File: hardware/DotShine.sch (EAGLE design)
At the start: 58 parts, among them CN1 1X4-BIG, IC1 CAT24M010TS, IC3 SI1145, J3 USB-MICROB, U1 ATMEGA328P-MU-QFN32, U2 TMP102, U3 ATSHA204-TSU, X2 MC-RTC-RV-4162-C7-I2C, X3 S4B-ZR

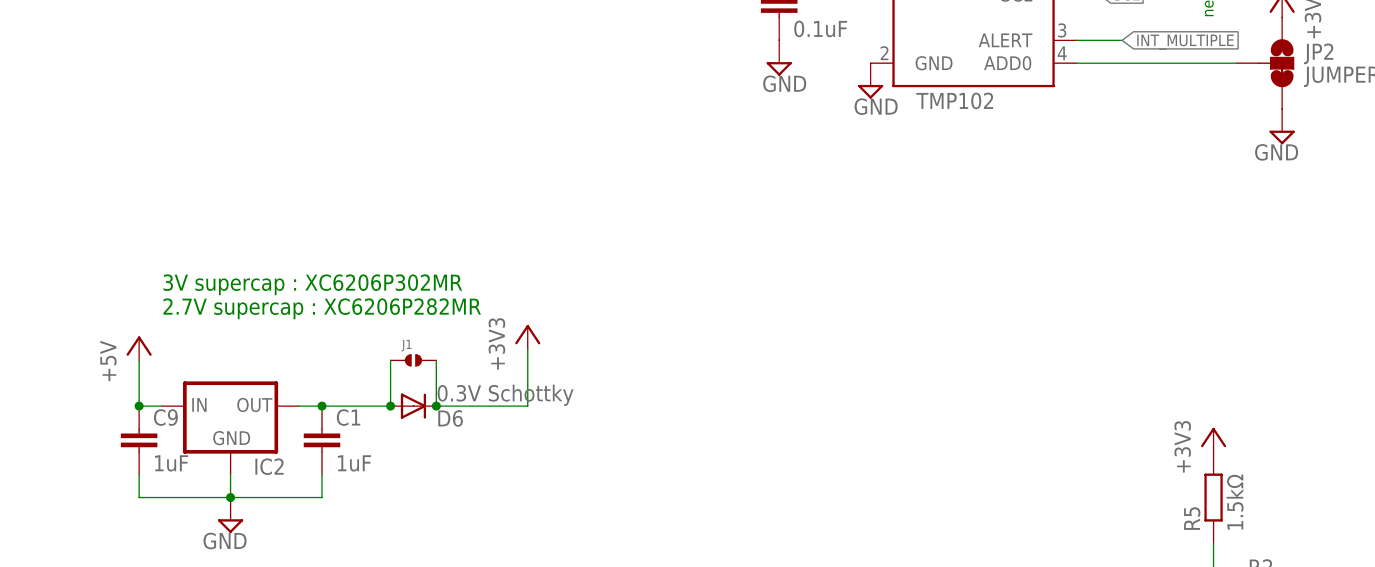
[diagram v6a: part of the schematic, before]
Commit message: Update LDO description
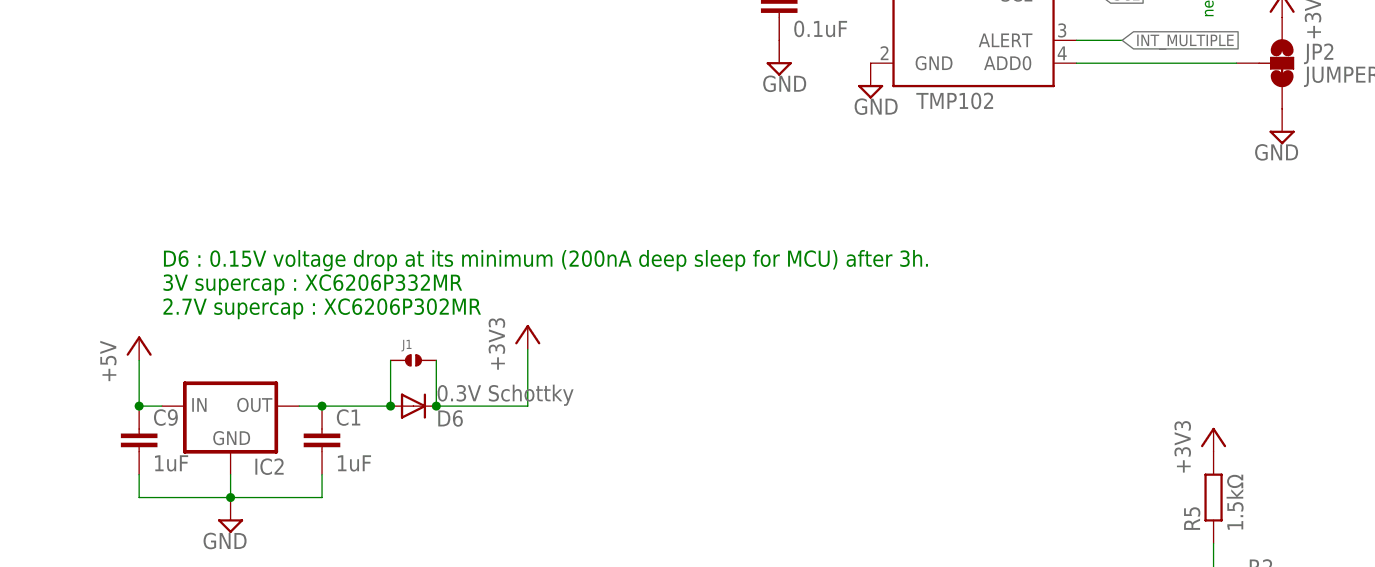
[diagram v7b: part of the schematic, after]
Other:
- note added: "D6 : 0.15V voltage drop at its minimum (200nA deep sleep for MCU) after 3h. 3V supercap : XC6206P332MR 2.7V supercap : XC6206P302MR"
- note removed: "3V supercap : XC6206P302MR 2.7V supercap : XC6206P282MR"
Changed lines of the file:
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@@
 <setting verticaltext="up"/>
 </settings>
-<grid distance="0.05" unitdist="inch" unit="inch" style="lines" multiple="1" display="no" altdistance="0.01" altunitdist="inch" altunit="inch"/>
+<grid distance="0.1" unitdist="inch" unit="inch" style="lines" multiple="1" display="no" altdistance="0.01" altunitdist="inch" altunit="inch"/>
 <layers>
 <layer number="1" name="Top" color="4" fill="1" visible="no" active="no"/>
@@
 <text x="30.48" y="-243.84" size="1.778" layer="91">1000uF .. 6V -&gt; 300uF .. 2V ; 600 .. 3.6V -&gt; buget: 600-300 = 300uF
 1500uF .. 4V -&gt; 750uF .. 2V ; 1350.. 3.6V-&gt; buget: 1350-750 = 600uF</text>
-<text x="137.16" y="-25.4" size="1.778" layer="91">3V supercap : XC6206P302MR
-2.7V supercap : XC6206P282MR</text>
+<text x="137.16" y="-25.4" size="1.778" layer="91">D6 : 0.15V voltage drop at its minimum (200nA deep sleep for MCU) after 3h.
+3V supercap : XC6206P332MR
+2.7V supercap : XC6206P302MR</text>
 <text x="248.92" y="-71.12" size="1.778" layer="91">5V Zener, otherwise
 leakage current too high </text>

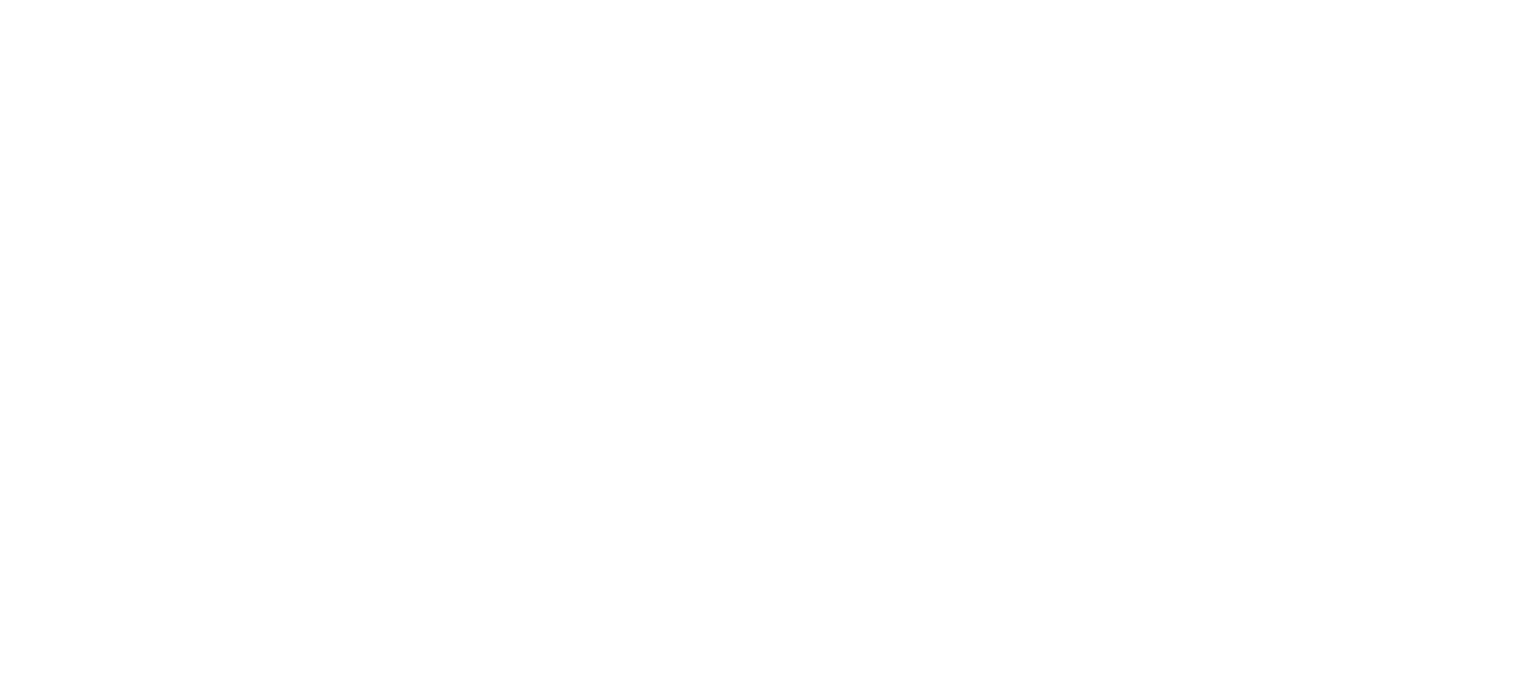
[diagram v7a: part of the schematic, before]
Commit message: Initial version with BLE using JDY-16
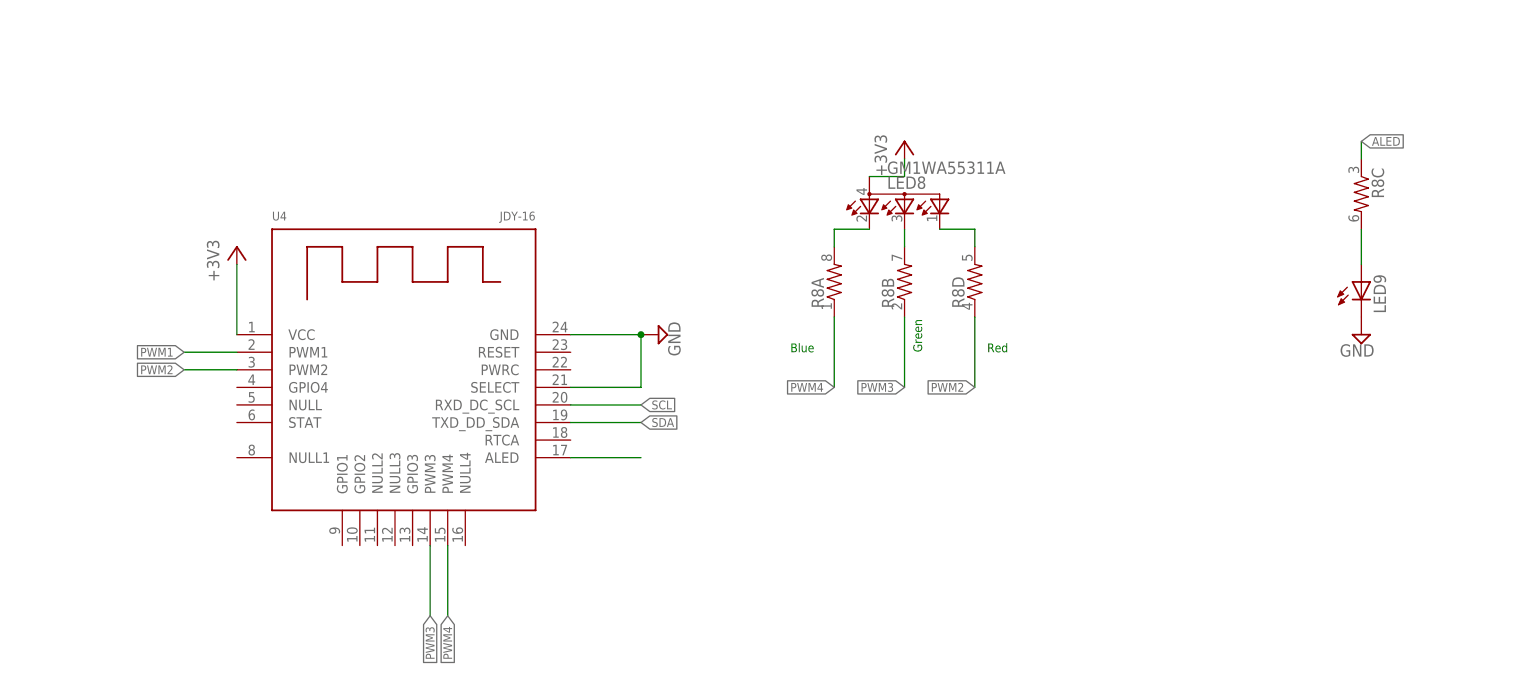
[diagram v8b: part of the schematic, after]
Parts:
- added LED8: GM1WA55311A, led:GM1WA55311A
- added LED9: (no value), SparkFun:LED0603
- added R8: (no value), SparkFun:RESISTOR-ARRAY0603-ARV
- added U4: JDY-16, altro:JDY-16
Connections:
- new net ALED: R8C.1, U4.ALED
- new net BT_BLUE: LED8.CRED, R8A.2
- new net BT_GREEN: LED8.CBLUE, R8B.2
- new net BT_RED: LED8.CGREEN, R8D.2
- new net N$34: LED9.A, R8C.2
- new net PWM1: U4.PWM1
- new net PWM2: R8D.1, U4.PWM2
- new net PWM3: R8B.1, U4.PWM3
- new net PWM4: R8A.1, U4.PWM4
- net +3V3: now also LED8.A, U4.VCC
- net GND: now also LED9.C, U4.GND, U4.SELECT
- net SCL: now also U4.RXD_DC_SCL
- net SDA: now also U4.TXD_DD_SDA
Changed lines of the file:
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@@
 <layer number="154" name="FabDoc2" color="2" fill="1" visible="no" active="no"/>
 <layer number="155" name="FabDoc3" color="7" fill="15" visible="no" active="no"/>
+<layer number="171" name="Fraes_2mm" color="7" fill="1" visible="no" active="yes"/>
 <layer number="199" name="Contour" color="7" fill="1" visible="no" active="no"/>
 <layer number="200" name="200bmp" color="1" fill="10" visible="yes" active="yes"/>
@@
 <part name="+3V17" library="supply1" deviceset="+3V3" device=""/>
 <part name="SUPPLY1" library="supply2" deviceset="GND" device=""/>
+<part name="U4" library="altro" deviceset="JDY-16" device=""/>
+<part name="+3V18" library="supply1" deviceset="+3V3" device=""/>
+<part name="LED8" library="led" deviceset="GM1WA55311A" device=""/>
+<part name="LED9" library="SparkFun" deviceset="LED" device="0603"/>
+<part name="SUPPLY8" library="supply2" deviceset="GND" device=""/>
+<part name="R8" library="SparkFun" deviceset="RESISTOR-ARRAY" device="0603-ARV"/>
+<part name="SUPPLY9" library="supply2" deviceset="GND" device=""/>
+<part name="+3V22" library="supply1" deviceset="+3V3" device=""/>
 </parts>
 <sheets>
@@
 leakage current too high </text>
 <text x="124.46" y="-147.32" size="1.27" layer="91">HW Reset with SW</text>
+<text x="175.26" y="-332.74" size="1.27" layer="91" rot="R90">Green</text>
+<text x="184.658" y="-332.74" size="1.27" layer="91">Red</text>
+<text x="156.21" y="-332.74" size="1.27" layer="91">Blue</text>
 </plain>
 <instances>
@@
 <instance part="+3V17" gate="G$1" x="162.56" y="132.08" rot="R270"/>
 <instance part="SUPPLY1" gate="GND" x="162.56" y="119.38" rot="R90"/>
+<instance part="U4" gate="G$1" x="101.6" y="-337.82"/>
+<instance part="+3V18" gate="G$1" x="172.72" y="-302.26"/>
+<instance part="LED8" gate="G$1" x="172.72" y="-309.88"/>
+<instance part="LED9" gate="G$1" x="238.76" y="-322.58"/>
+<instance part="SUPPLY8" gate="GND" x="238.76" y="-330.2" rot="MR0"/>
+<instance part="R8" gate="A" x="162.56" y="-322.58" rot="R90"/>
+<instance part="R8" gate="B" x="172.72" y="-322.58" rot="R90"/>
+<instance part="R8" gate="C" x="238.76" y="-309.88" rot="R270"/>
+<instance part="R8" gate="D" x="182.88" y="-322.58" rot="R90"/>
+<instance part="SUPPLY9" gate="GND" x="137.16" y="-330.2" rot="MR270"/>
+<instance part="+3V22" gate="G$1" x="76.2" y="-317.5"/>
 </instances>
 <busses>
@@
 <wire x1="160.02" y1="119.38" x2="142.24" y2="119.38" width="0.1524" layer="91"/>
 </segment>
+<segment>
+<pinref part="LED9" gate="G$1" pin="C"/>
+<pinref part="SUPPLY8" gate="GND" pin="GND"/>
+</segment>
+<segment>
+<pinref part="SUPPLY9" gate="GND" pin="GND"/>
+<pinref part="U4" gate="G$1" pin="GND"/>
+<wire x1="134.62" y1="-330.2" x2="124.46" y2="-330.2" width="0.1524" layer="91"/>
+<pinref part="U4" gate="G$1" pin="SELECT"/>
+<wire x1="124.46" y1="-337.82" x2="134.62" y2="-337.82" width="0.1524" layer="91"/>
+<wire x1="134.62" y1="-337.82" x2="134.62" y2="-330.2" width="0.1524" layer="91"/>
+<junction x="134.62" y="-330.2"/>
+</segment>
 </net>
 <net name="SDA" class="0">
@@
 <wire x1="170.18" y1="-210.82" x2="167.64" y2="-210.82" width="0.1524" layer="91"/>
 <label x="167.64" y="-210.82" size="1.27" layer="95" rot="R180" xref="yes"/>
+</segment>
+<segment>
+<pinref part="U4" gate="G$1" pin="TXD_DD_SDA"/>
+<wire x1="124.46" y1="-342.9" x2="134.62" y2="-342.9" width="0.1524" layer="91"/>
+<label x="134.62" y="-342.9" size="1.27" layer="95" xref="yes"/>
 </segment>
 </net>
@@
 <wire x1="160.02" y1="132.08" x2="142.24" y2="132.08" width="0.1524" layer="91"/>
 </segment>
+<segment>
+<pinref part="LED8" gate="G$1" pin="A"/>
+<pinref part="+3V18" gate="G$1" pin="+3V3"/>
+<wire x1="167.64" y1="-307.34" x2="172.72" y2="-307.34" width="0.1524" layer="91"/>
+<wire x1="172.72" y1="-307.34" x2="172.72" y2="-304.8" width="0.1524" layer="91"/>
+</segment>
+<segment>
+<pinref part="+3V22" gate="G$1" pin="+3V3"/>
+<pinref part="U4" gate="G$1" pin="VCC"/>
+<wire x1="76.2" y1="-320.04" x2="76.2" y2="-330.2" width="0.1524" layer="91"/>
+</segment>
 </net>
 <net name="ADCENA" class="0">
@@
 <wire x1="170.18" y1="-215.9" x2="167.64" y2="-215.9" width="0.1524" layer="91"/>
 <label x="167.64" y="-215.9" size="1.27" layer="95" rot="R180" xref="yes"/>
+</segment>
+<segment>
+<pinref part="U4" gate="G$1" pin="RXD_DC_SCL"/>
+<wire x1="124.46" y1="-340.36" x2="134.62" y2="-340.36" width="0.1524" layer="91"/>
+<label x="134.62" y="-340.36" size="1.27" layer="95" xref="yes"/>
 </segment>
 </net>
@@
 </segment>
 </net>
+<net name="BT_RED" class="0">
+<segment>
+<pinref part="R8" gate="D" pin="2"/>
+<pinref part="LED8" gate="G$1" pin="CGREEN"/>
+<wire x1="182.88" y1="-317.5" x2="182.88" y2="-314.96" width="0.1524" layer="91"/>
+<wire x1="182.88" y1="-314.96" x2="177.8" y2="-314.96" width="0.1524" layer="91"/>
+</segment>
+</net>
+<net name="N$34" class="0">
+<segment>
+<pinref part="R8" gate="C" pin="2"/>
+<pinref part="LED9" gate="G$1" pin="A"/>
+<wire x1="238.76" y1="-314.96" x2="238.76" y2="-320.04" width="0.1524" layer="91"/>
+</segment>
+</net>
+<net name="BT_GREEN" class="0">
+<segment>
+<pinref part="LED8" gate="G$1" pin="CBLUE"/>
+<pinref part="R8" gate="B" pin="2"/>
+<wire x1="172.72" y1="-317.5" x2="172.72" y2="-314.96" width="0.1524" layer="91"/>
+</segment>
+</net>
+<net name="BT_BLUE" class="0">
+<segment>
+<pinref part="LED8" gate="G$1" pin="CRED"/>
+<pinref part="R8" gate="A" pin="2"/>
+<wire x1="167.64" y1="-314.96" x2="162.56" y2="-314.96" width="0.1524" layer="91"/>
+<wire x1="162.56" y1="-314.96" x2="162.56" y2="-317.5" width="0.1524" layer="91"/>
+</segment>
+</net>
+<net name="PWM1" class="0">
+<segment>
+<pinref part="U4" gate="G$1" pin="PWM1"/>
+<wire x1="76.2" y1="-332.74" x2="68.58" y2="-332.74" width="0.1524" layer="91"/>
+<label x="68.58" y="-332.74" size="1.27" layer="95" rot="R180" xref="yes"/>
+</segment>
+</net>
+<net name="PWM2" class="0">
+<segment>
+<pinref part="U4" gate="G$1" pin="PWM2"/>
+<wire x1="76.2" y1="-335.28" x2="68.58" y2="-335.28" width="0.1524" layer="91"/>
+<label x="68.58" y="-335.28" size="1.27" layer="95" rot="R180" xref="yes"/>
+</segment>
+<segment>
+<pinref part="R8" gate="D" pin="1"/>
+<wire x1="182.88" y1="-327.66" x2="182.88" y2="-337.82" width="0.1524" layer="91"/>
+<label x="182.88" y="-337.82" size="1.27" layer="95" rot="R180" xref="yes"/>
+</segment>
+</net>
+<net name="PWM3" class="0">
+<segment>
+<pinref part="U4" gate="G$1" pin="PWM3"/>
+<wire x1="104.14" y1="-360.68" x2="104.14" y2="-370.84" width="0.1524" layer="91"/>
+<label x="104.14" y="-370.84" size="1.27" layer="95" rot="R270" xref="yes"/>
+</segment>
+<segment>
+<pinref part="R8" gate="B" pin="1"/>
+<wire x1="172.72" y1="-327.66" x2="172.72" y2="-337.82" width="0.1524" layer="91"/>
+<label x="172.72" y="-337.82" size="1.27" layer="95" rot="R180" xref="yes"/>
+</segment>
+</net>
+<net name="PWM4" class="0">
+<segment>
+<pinref part="U4" gate="G$1" pin="PWM4"/>
+<wire x1="106.68" y1="-360.68" x2="106.68" y2="-370.84" width="0.1524" layer="91"/>
+<label x="106.68" y="-370.84" size="1.27" layer="95" rot="R270" xref="yes"/>
+</segment>
+<segment>
+<pinref part="R8" gate="A" pin="1"/>
+<wire x1="162.56" y1="-327.66" x2="162.56" y2="-337.82" width="0.1524" layer="91"/>
+<label x="162.56" y="-337.82" size="1.27" layer="95" rot="R180" xref="yes"/>
+</segment>
+</net>
+<net name="ALED" class="0">
+<segment>
+<pinref part="R8" gate="C" pin="1"/>
+<wire x1="238.76" y1="-304.8" x2="238.76" y2="-302.26" width="0.1524" layer="91"/>
+<label x="238.76" y="-302.26" size="1.27" layer="95" xref="yes"/>
+</segment>
+<segment>
+<pinref part="U4" gate="G$1" pin="ALED"/>
+<wire x1="124.46" y1="-347.98" x2="134.62" y2="-347.98" width="0.1524" layer="91"/>
+</segment>
+</net>
